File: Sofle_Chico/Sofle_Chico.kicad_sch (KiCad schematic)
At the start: 121 parts, among them J1 Conn_01x05, J2 MJ-4PP-9, J3 Conn_01x04, J4 Conn_01x04, J5 Conn_01x05, J6 Conn_01x05, J7 Conn_01x04, Q1 DMG2305UX, SW1 SW_PUSH, SW10 SW_PUSH, SW11 SW_PUSH, SW12 SW_PUSH, SW13 SW_PUSH, SW14 SW_PUSH, SW15 SW_PUSH, SW16 SW_PUSH, SW17 SW_PUSH, SW18 SW_PUSH, SW19 SW_PUSH, SW2 SW_PUSH, SW20 SW_PUSH, SW21 SW_PUSH, SW22 SW_PUSH, SW23 SW_PUSH, SW24 SW_PUSH, SW25 Rotary_Encoder_Switch-Device, SW26 SW_PUSH, SW27 SW_PUSH, SW28 SW_PUSH, SW29 SW_PUSH, SW3 SW_PUSH, SW30 SW_PUSH, SW4 SW_PUSH, SW5 SW_PUSH, SW6 SW_PUSH, SW7 SW_PUSH, SW8 SW_PUSH, SW9 SW_PUSH, U1 SN74AHCT1G125, U2 Pico

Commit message: I2C Topology tweaking and tinkering from self review
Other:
- moved on the sheet: J1
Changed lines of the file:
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@@
   (no_connect (at 63.5 38.1))
   (no_connect (at 43.18 78.74))
-  (no_connect (at 69.85 166.37))
+  (no_connect (at 83.185 165.735))
   (no_connect (at 48.26 78.74))
   (no_connect (at 63.5 50.8))
@@
     (stroke (width 0) (type default))
   )
-  (wire (pts (xy 63.5 158.75) (xy 69.85 158.75))
+  (wire (pts (xy 76.835 158.115) (xy 83.185 158.115))
     (stroke (width 0) (type default))
   )
@@
     (stroke (width 0) (type default))
   )
+  (wire (pts (xy 68.58 163.195) (xy 83.185 163.195))
+    (stroke (width 0) (type default))
+  )
   (wire (pts (xy 26.67 160.02) (xy 22.86 160.02))
     (stroke (width 0) (type default))
@@
     (stroke (width 0) (type default))
   )
+  (wire (pts (xy 68.58 160.655) (xy 83.185 160.655))
+    (stroke (width 0) (type default))
+  )
   (wire (pts (xy 143.51 139.7) (xy 143.51 156.21))
     (stroke (width 0) (type default))
@@
     (stroke (width 0) (type default))
   )
-  (wire (pts (xy 64.77 168.91) (xy 69.85 168.91))
+  (wire (pts (xy 78.105 168.275) (xy 83.185 168.275))
     (stroke (width 0) (type default))
   )
@@
     (stroke (width 0) (type default))
   )
-  (wire (pts (xy 63.5 157.48) (xy 63.5 158.75))
+  (wire (pts (xy 76.835 156.845) (xy 76.835 158.115))
     (stroke (width 0) (type default))
   )
@@
     (fill (type none))
   )
-  (rectangle (start 60.96 151.13) (end 85.09 175.26)
+  (rectangle (start 60.96 151.13) (end 97.155 175.26)
     (stroke (width 0) (type default))
     (fill (type none))
@@
     )
   )
-  (global_label "SCL" (shape input) (at 69.85 163.83 180) (fields_autoplaced)
-    (effects (font (size 1.27 1.27)) (justify right))
-    (property "Intersheetrefs" "${INTERSHEET_REFS}" (at 63.4366 163.83 0)
-      (effects (font (size 1.27 1.27)) (justify right) hide)
-    )
-  )
   (global_label "col2" (shape input) (at 204.47 90.17 90)
     (effects (font (size 1.27 1.27)) (justify left))
@@
     )
   )
-  (global_label "SDA" (shape input) (at 69.85 161.29 180) (fields_autoplaced)
-    (effects (font (size 1.27 1.27)) (justify right))
-    (property "Intersheetrefs" "${INTERSHEET_REFS}" (at 63.3761 161.29 0)
-      (effects (font (size 1.27 1.27)) (justify right) hide)
-    )
-  )
   (global_label "GP19" (shape input) (at 43.18 157.48 0) (fields_autoplaced)
     (effects (font (size 1.27 1.27)) (justify left))
@@
     )
   )
+  (global_label "SCL" (shape input) (at 68.58 163.195 180) (fields_autoplaced)
+    (effects (font (size 1.27 1.27)) (justify right))
+    (property "Intersheetrefs" "${INTERSHEET_REFS}" (at 62.1666 163.195 0)
+      (effects (font (size 1.27 1.27)) (justify right) hide)
+    )
+  )
   (global_label "row3" (shape input) (at 140.97 147.32 180)
     (effects (font (size 1.27 1.27)) (justify right))
@@
     )
   )
+  (global_label "SDA" (shape input) (at 68.58 160.655 180) (fields_autoplaced)
+    (effects (font (size 1.27 1.27)) (justify right))
+    (property "Intersheetrefs" "${INTERSHEET_REFS}" (at 62.1061 160.655 0)
+      (effects (font (size 1.27 1.27)) (justify right) hide)
+    )
+  )
   (global_label "3V3" (shape input) (at 54.61 96.52 0) (fields_autoplaced)
     (effects (font (size 1.27 1.27)) (justify left))
@@
     )
   )
-  (symbol (lib_id "power:GND") (at 64.77 168.91 0) (unit 1)
+  (symbol (lib_id "power:GND") (at 78.105 168.275 0) (unit 1)
     (in_bom yes) (on_board yes) (dnp no) (fields_autoplaced)
-    (property "Reference" "#PWR023" (at 64.77 175.26 0)
+    (property "Reference" "#PWR023" (at 78.105 174.625 0)
       (effects (font (size 1.27 1.27)) hide)
     )
-    (property "Value" "GND" (at 64.77 173.99 0)
+    (property "Value" "GND" (at 78.105 173.355 0)
       (effects (font (size 1.27 1.27)))
     )
-    (property "Footprint" "" (at 64.77 168.91 0)
+    (property "Footprint" "" (at 78.105 168.275 0)
       (effects (font (size 1.27 1.27)) hide)
     )
-    (property "Datasheet" "" (at 64.77 168.91 0)
+    (property "Datasheet" "" (at 78.105 168.275 0)
       (effects (font (size 1.27 1.27)) hide)
     )
@@
     )
   )
-  (symbol (lib_id "Sofle_Pico:Conn_01x05") (at 74.93 163.83 0) (unit 1)
+  (symbol (lib_id "Sofle_Pico:Conn_01x05") (at 88.265 163.195 0) (unit 1)
     (in_bom no) (on_board yes) (dnp no)
-    (property "Reference" "J1" (at 74.93 156.21 0)
+    (property "Reference" "J1" (at 88.265 155.575 0)
       (effects (font (size 1.27 1.27)))
     )
-    (property "Value" "Conn_01x05" (at 74.93 171.45 0)
+    (property "Value" "Conn_01x05" (at 88.265 170.815 0)
       (effects (font (size 1.27 1.27)))
     )
-    (property "Footprint" "Sofle_Pico:Pimaroni_PinHeader_1x05_P2.54mm_Vertical Sofle v3b" (at 74.93 163.83 0)
+    (property "Footprint" "Sofle_Pico:Pimaroni_PinHeader_1x05_P2.54mm_Vertical Sofle v3b" (at 88.265 163.195 0)
       (effects (font (size 1.27 1.27)) hide)
     )
-    (property "Datasheet" "~" (at 74.93 163.83 0)
+    (property "Datasheet" "~" (at 88.265 163.195 0)
       (effects (font (size 1.27 1.27)) hide)
     )
@@
     )
   )
-  (symbol (lib_id "power:VDC") (at 63.5 157.48 0) (unit 1)
+  (symbol (lib_id "power:VDC") (at 76.835 156.845 0) (unit 1)
     (in_bom yes) (on_board yes) (dnp no) (fields_autoplaced)
-    (property "Reference" "#PWR05" (at 63.5 161.29 0)
+    (property "Reference" "#PWR05" (at 76.835 160.655 0)
       (effects (font (size 1.27 1.27)) hide)
     )
-    (property "Value" "VDC" (at 66.04 156.21 0)
+    (property "Value" "VDC" (at 79.375 155.575 0)
       (effects (font (size 1.27 1.27)))
     )
-    (property "Footprint" "" (at 63.5 157.48 0)
+    (property "Footprint" "" (at 76.835 156.845 0)
       (effects (font (size 1.27 1.27)) hide)
     )
-    (property "Datasheet" "" (at 63.5 157.48 0)
+    (property "Datasheet" "" (at 76.835 156.845 0)
       (effects (font (size 1.27 1.27)) hide)
     )

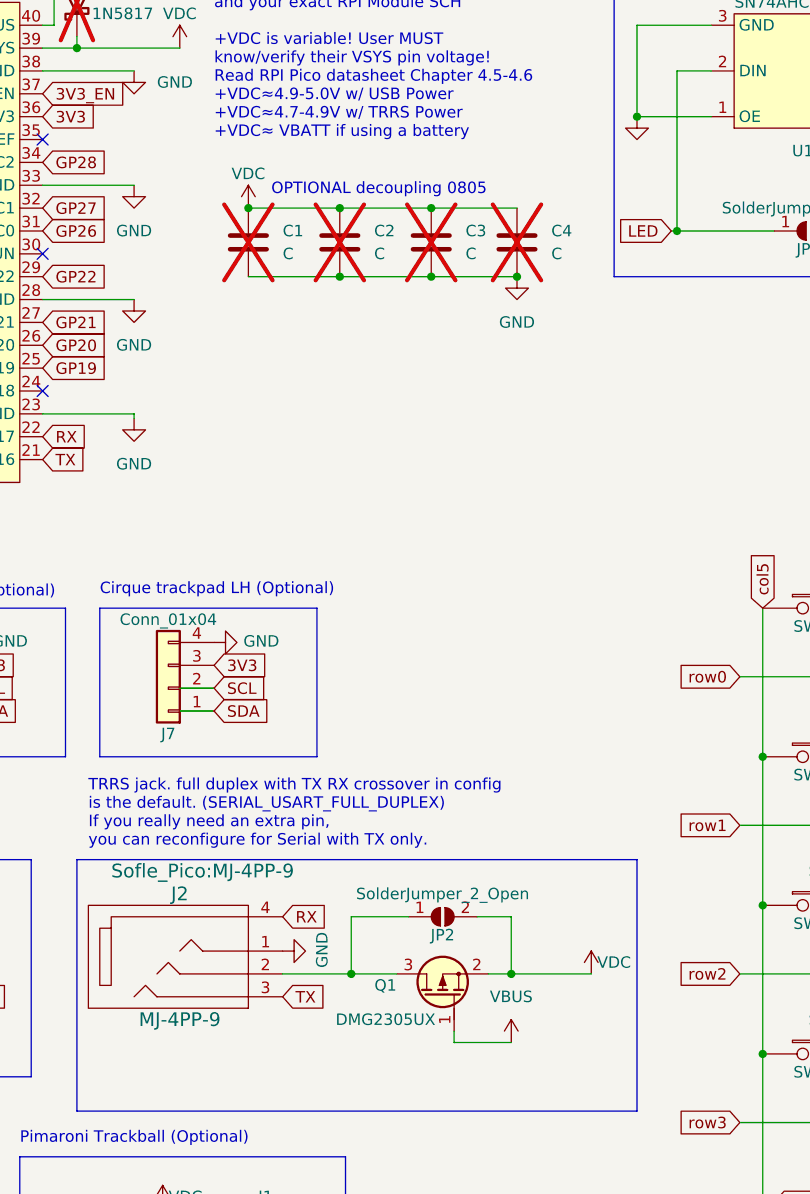
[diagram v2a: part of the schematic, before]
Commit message: added LH/RH outline logos, removed socket notation marks
Updated Choc switch library for first attempt at keyplate aperture SVG lines, now I gotta learn 3D conversion method
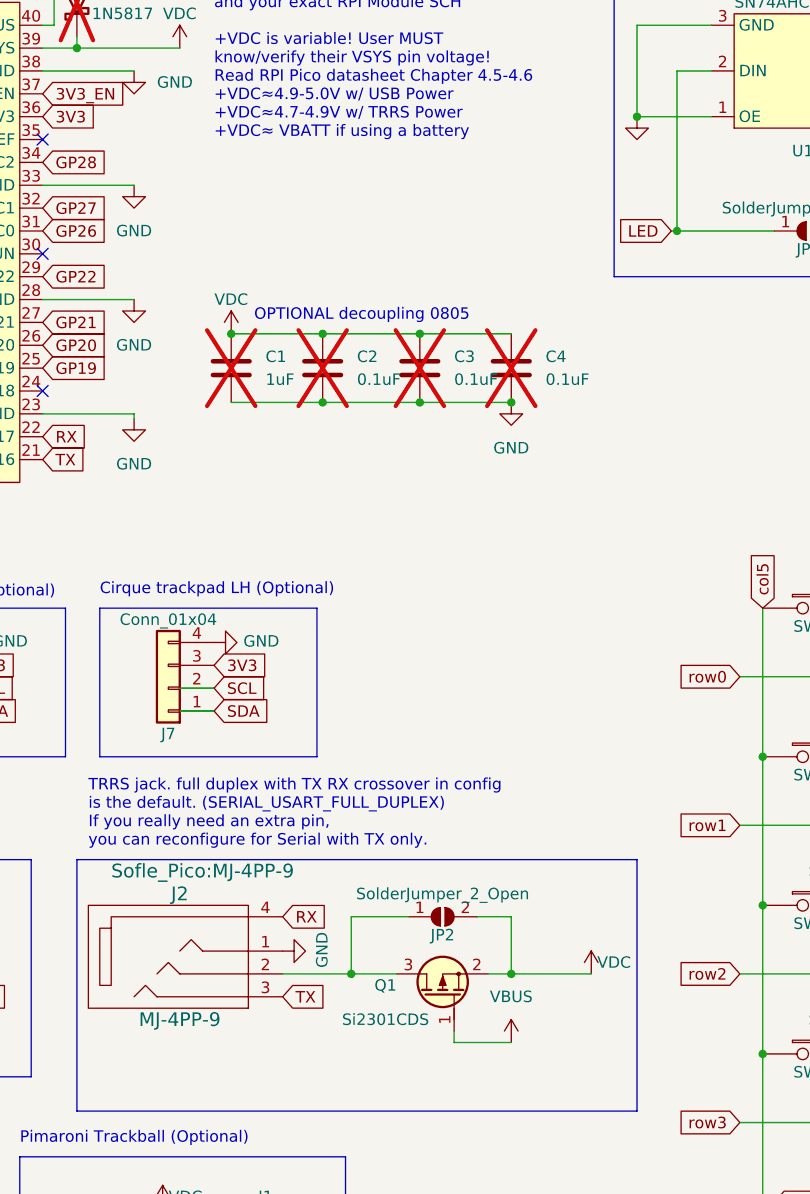
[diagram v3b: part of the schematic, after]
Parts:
- C1: value C -> 1uF; Dielectric (none) -> X7R; MFG (none) -> Samsung; MFG PN (none) -> CL21B105KBFNNNE; Tolerance (%) (none) -> 10; Voltage Rating (none) -> 50V
- C2, C3, C4: value C -> 0.1uF; Dielectric (none) -> X7R; MFG (none) -> YAGEO; MFG PN (none) -> CC0805KRX7R9BB104; Tolerance (%) (none) -> 10; Voltage Rating (none) -> 50V
- Q1: value DMG2305UX -> Si2301CDS
- TH1, TH2, TH7: footprint Sofle_Pico:keyplate_hole_M2_standoff_passthrough -> Sofle_Pico:Hole from sofle for M2 posts gold rimmer wide-keyplate-hole
- TH3, TH4, TH6, TH8: footprint Sofle_Pico:keyplate_hole_M2_standoff_passthrough -> Sofle_Pico:Hole from sofle for M2 posts gold rimmer
- TH5: footprint (none) -> Sofle_Pico:Hole from sofle for M2 posts gold rimmer
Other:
- moved on the sheet: C1

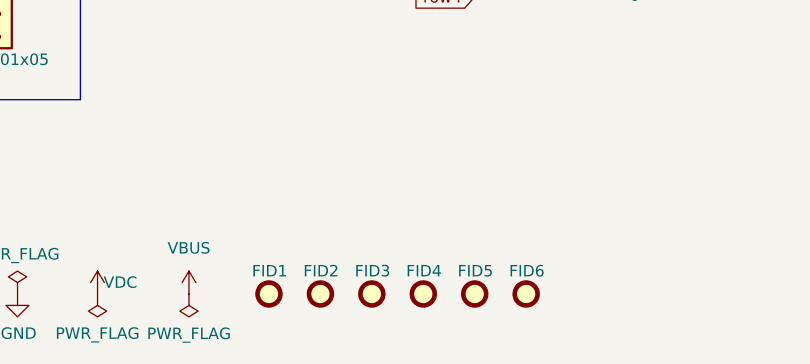
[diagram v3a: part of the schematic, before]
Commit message: Added soldermask pullbacks to board edges with manual lines on F./B.Mask layers
Started updating SCH to use JLCPCB standard stocked parts for PFET/diodes/caps (need to look for level shifter)

Added left/right hand outline for handedness quick reference

Updated Chico boards to have keyplate SVG lines for chocv1
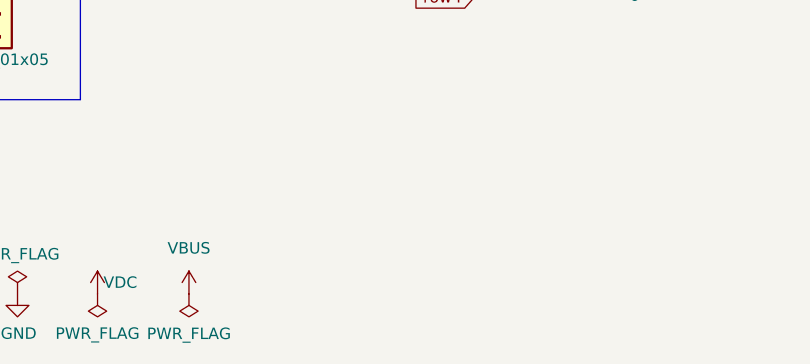
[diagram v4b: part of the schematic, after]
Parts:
- removed FID1, FID2, FID3, FID4, FID5, FID6: Fiducial, Fiducial:Fiducial_0.5mm_Mask1.5mm, symbol Mechanical:Fiducial
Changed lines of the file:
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@@
-    )
-  )
-  (symbol (lib_id "Mechanical:Fiducial") (at 123.825 196.85 0) (unit 1)
-    (in_bom yes) (on_board yes) (dnp no)
-    (property "Reference" "FID2" (at 121.92 194.31 0)
-      (effects (font (size 1.27 1.27)) (justify left))
-    )
-    (property "Value" "Fiducial" (at 125.984 198.0621 0)
-      (effects (font (size 1.27 1.27)) (justify left) hide)
-    )
-    (property "Footprint" "Fiducial:Fiducial_0.5mm_Mask1.5mm" (at 123.825 196.85 0)
-      (effects (font (size 1.27 1.27)) hide)
-    )
-    (property "Datasheet" "~" (at 123.825 196.85 0)
-      (effects (font (size 1.27 1.27)) hide)
-    )
-    (instances
-      (project "Sofle_Chico"
-        (path "/06057b3a-55ab-4f4e-913e-2aeec5ff3587"
-          (reference "FID2") (unit 1)
-        )
-      )
     )
   )
@@
         (path "/06057b3a-55ab-4f4e-913e-2aeec5ff3587"
           (reference "#PWR0113") (unit 1)
-        )
-      )
-    )
-  )
-  (symbol (lib_id "Mechanical:Fiducial") (at 146.685 196.85 0) (unit 1)
-    (in_bom yes) (on_board yes) (dnp no)
-    (property "Reference" "FID6" (at 144.78 194.31 0)
-      (effects (font (size 1.27 1.27)) (justify left))
-    )
-    (property "Value" "Fiducial" (at 148.844 198.0621 0)
-      (effects (font (size 1.27 1.27)) (justify left) hide)
-    )
-    (property "Footprint" "Fiducial:Fiducial_0.5mm_Mask1.5mm" (at 146.685 196.85 0)
-      (effects (font (size 1.27 1.27)) hide)
-    )
-    (property "Datasheet" "~" (at 146.685 196.85 0)
-      (effects (font (size 1.27 1.27)) hide)
-    )
-    (instances
-      (project "Sofle_Chico"
-        (path "/06057b3a-55ab-4f4e-913e-2aeec5ff3587"
-          (reference "FID6") (unit 1)
         )
       )
@@
     )
   )
-  (symbol (lib_id "Mechanical:Fiducial") (at 135.255 196.85 0) (unit 1)
-    (in_bom yes) (on_board yes) (dnp no)
-    (property "Reference" "FID4" (at 133.35 194.31 0)
-      (effects (font (size 1.27 1.27)) (justify left))
-    )
-    (property "Value" "Fiducial" (at 137.414 198.0621 0)
-      (effects (font (size 1.27 1.27)) (justify left) hide)
-    )
-    (property "Footprint" "Fiducial:Fiducial_0.5mm_Mask1.5mm" (at 135.255 196.85 0)
-      (effects (font (size 1.27 1.27)) hide)
-    )
-    (property "Datasheet" "~" (at 135.255 196.85 0)
-      (effects (font (size 1.27 1.27)) hide)
-    )
-    (instances
-      (project "Sofle_Chico"
-        (path "/06057b3a-55ab-4f4e-913e-2aeec5ff3587"
-          (reference "FID4") (unit 1)
-        )
-      )
-    )
-  )
   (symbol (lib_name "GND_3") (lib_id "power:GND") (at 73.66 43.18 0) (unit 1)
     (in_bom yes) (on_board yes) (dnp no) (fields_autoplaced)
@@
         (path "/06057b3a-55ab-4f4e-913e-2aeec5ff3587"
           (reference "J6") (unit 1)
-        )
-      )
-    )
-  )
-  (symbol (lib_id "Mechanical:Fiducial") (at 140.97 196.85 0) (unit 1)
-    (in_bom yes) (on_board yes) (dnp no)
-    (property "Reference" "FID5" (at 139.065 194.31 0)
-      (effects (font (size 1.27 1.27)) (justify left))
-    )
-    (property "Value" "Fiducial" (at 143.129 198.0621 0)
-      (effects (font (size 1.27 1.27)) (justify left) hide)
-    )
-    (property "Footprint" "Fiducial:Fiducial_0.5mm_Mask1.5mm" (at 140.97 196.85 0)
-      (effects (font (size 1.27 1.27)) hide)
-    )
-    (property "Datasheet" "~" (at 140.97 196.85 0)
-      (effects (font (size 1.27 1.27)) hide)
-    )
-    (instances
-      (project "Sofle_Chico"
-        (path "/06057b3a-55ab-4f4e-913e-2aeec5ff3587"
-          (reference "FID5") (unit 1)
         )
       )
@@
     )
   )
-  (symbol (lib_id "Mechanical:Fiducial") (at 118.11 196.85 0) (unit 1)
-    (in_bom yes) (on_board yes) (dnp no)
-    (property "Reference" "FID1" (at 116.205 194.31 0)
-      (effects (font (size 1.27 1.27)) (justify left))
-    )
-    (property "Value" "Fiducial" (at 120.269 198.0621 0)
-      (effects (font (size 1.27 1.27)) (justify left) hide)
-    )
-    (property "Footprint" "Fiducial:Fiducial_0.5mm_Mask1.5mm" (at 118.11 196.85 0)
-      (effects (font (size 1.27 1.27)) hide)
-    )
-    (property "Datasheet" "~" (at 118.11 196.85 0)
-      (effects (font (size 1.27 1.27)) hide)
-    )
-    (instances
-      (project "Sofle_Chico"
-        (path "/06057b3a-55ab-4f4e-913e-2aeec5ff3587"
-          (reference "FID1") (unit 1)
-        )
-      )
-    )
-  )
   (symbol (lib_id "power:VDC") (at 201.93 30.48 0) (unit 1)
     (in_bom yes) (on_board yes) (dnp no)
@@
         )
       )
-    )
-  )
-  (symbol (lib_id "Mechanical:Fiducial") (at 129.54 196.85 0) (unit 1)
-    (in_bom yes) (on_board yes) (dnp no)
-    (property "Reference" "FID3" (at 127.635 194.31 0)
-      (effects (font (size 1.27 1.27)) (justify left))
-    )
-    (property "Value" "Fiducial" (at 131.699 198.0621 0)
-      (effects (font (size 1.27 1.27)) (justify left) hide)
-    )
-    (property "Footprint" "Fiducial:Fiducial_0.5mm_Mask1.5mm" (at 129.54 196.85 0)
-      (effects (font (size 1.27 1.27)) hide)
-    )
-    (property "Datasheet" "~" (at 129.54 196.85 0)
-      (effects (font (size 1.27 1.27)) hide)
-    )
-    (instances
-      (project "Sofle_Chico"
-        (path "/06057b3a-55ab-4f4e-913e-2aeec5ff3587"
-          (reference "FID3") (unit 1)
-        )
-      )

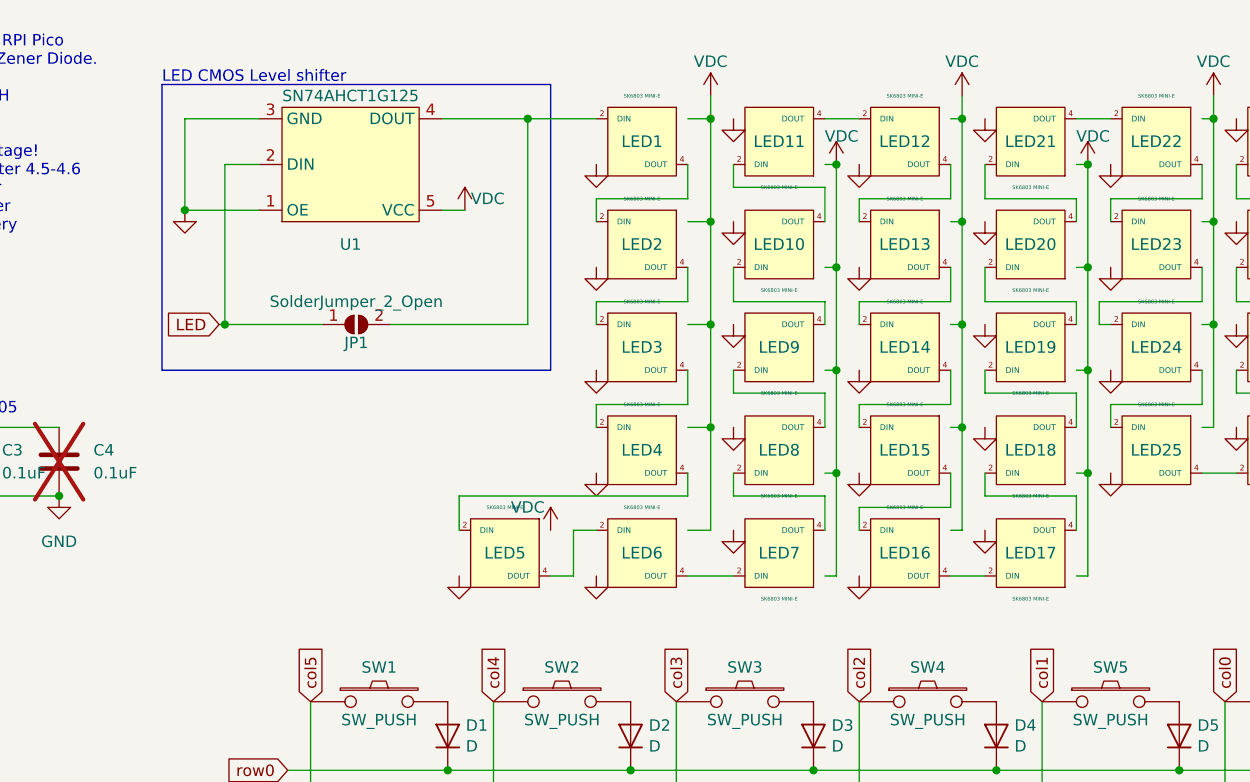
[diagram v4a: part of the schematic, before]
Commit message: Fixed overlapping holes in MX footprint that generated incorrect drill hit tables
Opened jumper soldermask apertures to allow for easier drag-solder bridging

Updated SCH to new buffer for JLCPCB "basic" part

Added JLCPCB PN params to parts for "basic" parts

Copied edge soldermask pullbacks from pico to chico
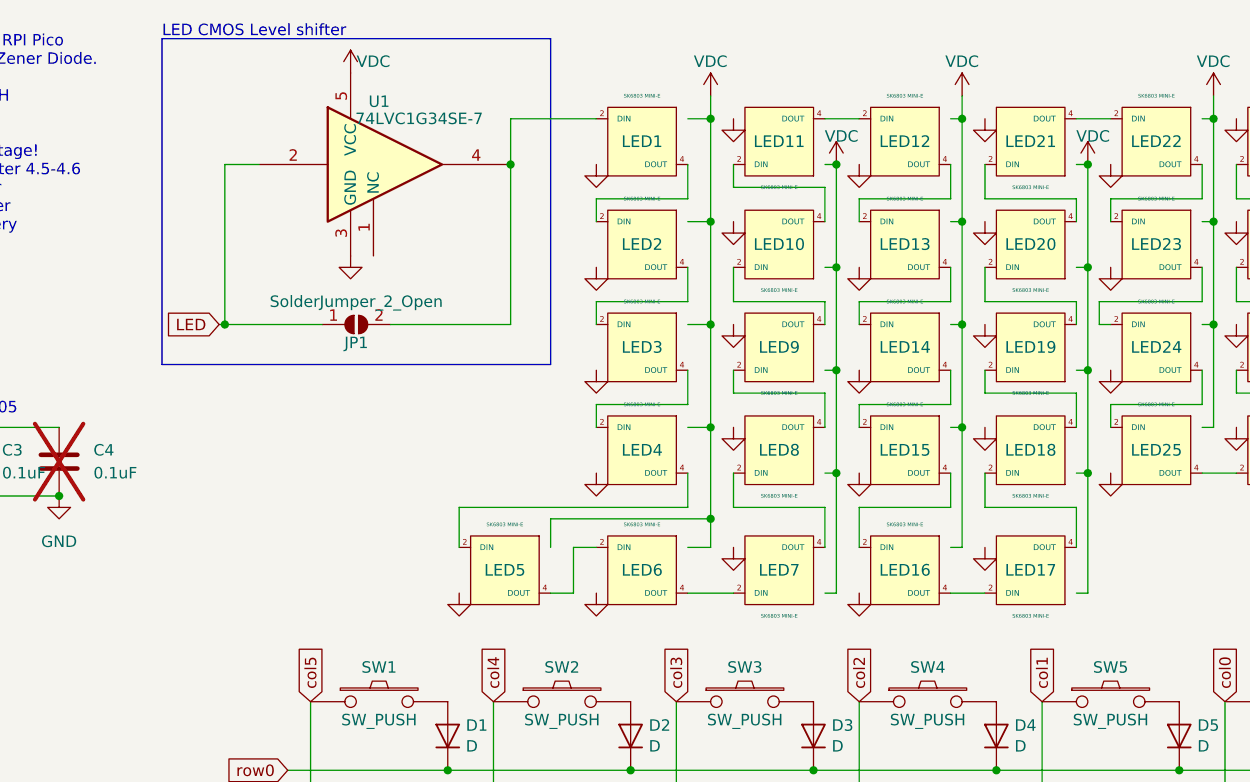
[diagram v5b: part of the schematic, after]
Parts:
- removed U1: SN74AHCT1G125, PCM_Package_TO_SOT_SMD_AKL:SOT-23-5_HandSoldering, symbol Sofle_Pico:SN74AHCT1G125
- added U1: 74LVC1G34SE-7, Package_TO_SOT_SMD:SOT-353_SC-70-5_Handsoldering, symbol 74xGxx:74LVC1G34
- C1: JLCPCB_PN (none) -> C28323
- C2, C3, C4: JLCPCB_PN (none) -> C49678
- D1, D10, D11, D12, D13, D14, D15, D16, D17, D18, D19, D2, D20, D21, D22, D23, D24, D25, D26, D27, D28, D29, D3, D30, D4, D5, D6, D7, D8, D9: JLCPCB_PN (none) -> C81598; MFG (none) -> Semtech; MFG PN (none) -> 1N4148W; Voltage Rating (none) -> 75v
- Q1: JLCPCB_PN (none) -> C10487
- TP1: JLCPCB_PN (none) -> C94111
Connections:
- net GND: now also U1.3 (GND)
- net LED: now also U1.2
- net VDC: now also U1.5 (VCC)
- net at JP1.2 (B), LED1.2 (DIN): now also U1.4
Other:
- title: Sofle Pico -> Sofle Pico Choc
- moved on the sheet: LED16, LED17, LED5, LED6, LED7
